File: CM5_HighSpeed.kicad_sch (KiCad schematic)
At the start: 60 parts, among them J1 USB-C, J10 USB-C, J15 USB_C_Receptacle, J17 USB-C, J22 Conn_HDMI, J5 Conn_1x22_Female, J6 USB-C, U11 TUSB4041I, U12 RT9742SNGV, U13 TLV73311PDBV, U15 AP22653W6, U6 AP22653W6, Y1 ECS-2520MV-240-CN-TR

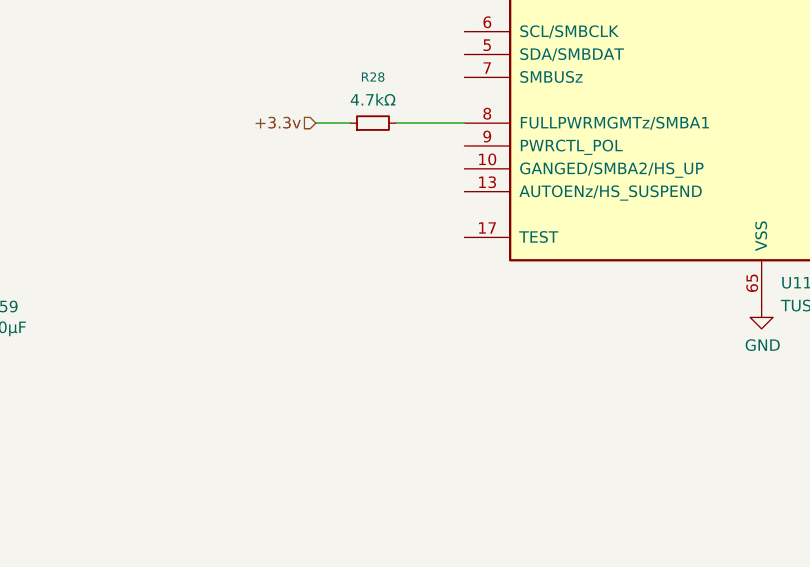
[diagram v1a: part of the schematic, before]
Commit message: USB hub: pull TEST (U11 pin 17) to GND through 4.7k
Pin 17 was left floating. It has an internal pull-down, but TI's
application circuit (TUSB4041I datasheet, Figure 7-8) pulls it down
externally with 4.7k, so follow the reference design.

New R47: 4.7k 1% 0603, Panasonic ERJ-3EKF4701V.

Refs #26 (verify on hardware before closing).

Co-Authored-By: Claude Opus 5.5 <noreply@anthropic.com>
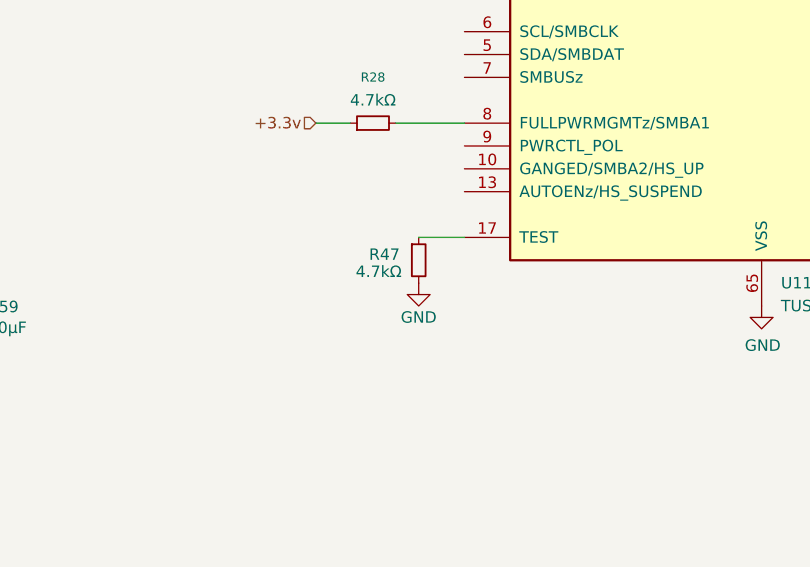
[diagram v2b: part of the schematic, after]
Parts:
- added R47: 4.7kΩ, Resistor_SMD:R_0603_1608Metric, symbol Device:R_Small
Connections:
- net GND: now also R47.2
- net at U11.17 (TEST): now also R47.1
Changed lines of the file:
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@@
 	(wire
 		(pts
+			(xy 210.82 204.47) (xy 215.9 204.47)
+		)
+		(stroke
+			(width 0)
+			(type default)
+		)
+	)
+	(wire
+		(pts
 			(xy 148.59 25.4) (xy 148.59 33.02)
 		)
@@
 	(symbol
 		(lib_id "power:GND")
+		(at 210.82 209.55 0)
+		(unit 1)
+		(body_style 1)
+		(exclude_from_sim no)
+		(in_bom yes)
+		(on_board yes)
+		(in_pos_files yes)
+		(dnp no)
+		(property "Reference" "#PWR002"
+			(at 210.82 215.9 0)
+			(hide yes)
+			(show_name no)
+			(do_not_autoplace no)
+			(effects
+				(font
+					(size 1.27 1.27)
+				)
+			)
+		)
+		(property "Value" "GND"
+			(at 210.82 213.36 0)
+			(show_name no)
+			(do_not_autoplace no)
+			(effects
+				(font
+					(size 1.27 1.27)
+				)
+			)
+		)
+		(property "Footprint" ""
+			(at 210.82 209.55 0)
+			(hide yes)
+			(show_name no)
+			(do_not_autoplace no)
+			(effects
+				(font
+					(size 1.27 1.27)
+				)
+			)
+		)
+		(property "Datasheet" ""
+			(at 210.82 209.55 0)
+			(hide yes)
+			(show_name no)
+			(do_not_autoplace no)
+			(effects
+				(font
+					(size 1.27 1.27)
+				)
+			)
+		)
+		(property "Description" "Power symbol creates a global label with name \"GND\" , ground"
+			(at 210.82 209.55 0)
+			(hide yes)
+			(show_name no)
+			(do_not_autoplace no)
+			(effects
+				(font
+					(size 1.27 1.27)
+				)
+			)
+		)
+		(pin "1"
+		)
+		(instances
+			(project "libreboard"
+				(path "/e63e39d7-6ac0-4ffd-8aa3-1841a4541b55/00000000-0000-0000-0000-00005cff70b1"
+					(reference "#PWR002")
+					(unit 1)
+				)
+			)
+		)
+	)
+	(symbol
+		(lib_id "power:GND")
 		(at 62.23 255.27 0)
 		(unit 1)
@@
 					(unit 1)
 				)
+			)
+		)
+	)
+	(symbol
+		(lib_id "Device:R_Small")
+		(at 210.82 207.01 0)
+		(unit 1)
+		(body_style 1)
+		(exclude_from_sim no)
+		(in_bom yes)
+		(on_board yes)
+		(in_pos_files yes)
+		(dnp no)
+		(property "Reference" "R47"
+			(at 207.01 206.375 0)
+			(show_name no)
+			(do_not_autoplace no)
+			(effects
+				(font
+					(size 1.27 1.27)
+				)
+			)
+		)
+		(property "Value" "4.7kΩ"
+			(at 206.375 208.28 0)
+			(show_name no)
+			(do_not_autoplace no)
+			(effects
+				(font
+					(size 1.27 1.27)
+				)
+			)
+		)
+		(property "Footprint" "Resistor_SMD:R_0603_1608Metric"
+			(at 210.82 207.01 0)
+			(hide yes)
+			(show_name no)
+			(do_not_autoplace no)
+			(effects
+				(font
+					(size 1.27 1.27)
+				)
+			)
+		)
+		(property "Datasheet" ""
+			(at 210.82 207.01 0)
+			(hide yes)
+			(show_name no)
+			(do_not_autoplace no)
+			(effects
+				(font
+					(size 1.27 1.27)
+				)
+			)
+		)
+		(property "Description" "Resistor, small symbol"
+			(at 210.82 207.01 0)
+			(hide yes)
+			(show_name no)
+			(do_not_autoplace no)
+			(effects
+				(font
+					(size 1.27 1.27)
+				)
+			)
+		)
+		(property "Dist. P/N" "P4.70KHTR-ND"
+			(at 210.82 207.01 0)
+			(hide yes)
+			(show_name no)
+			(do_not_autoplace no)
+			(effects
+				(font
+					(size 1.27 1.27)
+				)
+			)
+		)
+		(property "Distributor" "Digikey"
+			(at 210.82 207.01 0)
+			(hide yes)
+			(show_name no)
+			(do_not_autoplace no)
+			(effects
+				(font
+					(size 1.27 1.27)
+				)
+			)
+		)
+		(property "Manf. P/N" "ERJ-3EKF4701V"
+			(at 210.82 207.01 0)
+			(hide yes)
+			(show_name no)
+			(do_not_autoplace no)
+			(effects
+				(font
+					(size 1.27 1.27)
+				)
+			)
+		)
+		(property "Manufacturer" "Panasonic"
+			(at 210.82 207.01 0)
+			(hide yes)
+			(show_name no)
+			(do_not_autoplace no)
+			(effects
+				(font
+					(size 1.27 1.27)
+				)
+			)
+		)
+		(property "Part Description" "Resistor, 4.7kΩ, ±1%, 0.1W, SMD 0603 (1608m)"
+			(at 210.82 207.01 0)
+			(hide yes)
+			(show_name no)
+			(do_not_autoplace no)
+			(effects
+				(font
+					(size 1.27 1.27)
+				)
+			)
+		)
+		(pin "1"
+		)
+		(pin "2"
+		)
+		(instances
+			(project "libreboard"
+				(path "/e63e39d7-6ac0-4ffd-8aa3-1841a4541b55/00000000-0000-0000-0000-00005cff70b1"
+					(reference "R47")
+					(unit 1)
+				)

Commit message: USB hub: divide VBUS down before U11 USB_VBUS (pin 16)
U11 pin 16 was tied straight to the 5 V USB2_VBUS rail. Its absolute
maximum is 1.4 V and the recommended maximum 1.155 V (TUSB4041I
datasheet 5.1/5.3); the pin function table requires a 90.9k/10k 1%
divider. Continuous overstress of this pin is the most likely reason
the Rev1 hub worked for a while and then never enumerated again.

New R48 90.9k (ERJ-3EKF9092V) from USB2_VBUS and R49 10k (ERJ-3EKF1002V)
to GND, 0603; the midpoint feeds pin 16 through the HUB_VBUS_DET label.
5.0 V gives 0.495 V, 5.5 V gives 0.545 V at the pin.

Refs #23 (verify on hardware before closing).

Co-Authored-By: Claude Opus 5.5 <noreply@anthropic.com>
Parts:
- added R48: 90.9kΩ, Resistor_SMD:R_0603_1608Metric, symbol Device:R_Small
- added R49: 10kΩ, Resistor_SMD:R_0603_1608Metric, symbol Device:R_Small
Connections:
- net GND: now also R49.2
- net USB2_VBUS: now also R48.1; no longer U11.16 (USB_VBUS)
- new net HUB_VBUS_DET: R48.2, R49.1, U11.16 (USB_VBUS)

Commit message: USB hub: run the 24 MHz oscillator Y1 from the CM5 1.8 V output
Y1 (ECS-2520MV, 1.6-3.6 V supply) was powered from +3.3 V and drove
U11 XI (pin 30) with a 3.3 V clock. XI is rated 2.45 V absolute maximum
and TI requires a 1.8 V clock source (TUSB4041I datasheet 5.1, 6.3.6).

- Y1 VDD and its decoupling cap C50 move from +3.3v to a new +1V8 net.
- +1V8 comes from the CM5's +1.8 V output pins 88/90 (600 mA total),
  which were unused (no-connect flags removed).
- Y1 tri-state pin 1 gets a no-connect flag: open = output enabled per
  the ECS-2520MV datasheet.

Note: Y1's Value field says ECS-2520MV-240-CN-TR while its MPN/Digikey
fields say -DN-TR (C = +/-25 ppm, D = +/-20 ppm); both meet the hub's
+/-100 ppm. Left as is for the BOM owner to reconcile.

Refs #24 (verify on hardware before closing).

Co-Authored-By: Claude Opus 5.5 <noreply@anthropic.com>
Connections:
- net +3.3v: no longer C50.2, Y1.4 (VDD)
- new net +1V8: C50.2, Y1.4 (VDD)
- no-connect marks 3 -> 4
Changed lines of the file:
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@@
 		(at 254 66.04)
 	)
+	(no_connect
+		(at 151.13 160.02)
+	)
 	(wire
 		(pts
@@
 		)
 	)
-	(hierarchical_label "+3.3v"
-		(shape input)
-		(at 135.89 146.05 180)
-		(effects
-			(font
-				(size 1.27 1.27)
-			)
-			(justify right)
-		)
-	)
 	(hierarchical_label "PCIE_nCLKREQ"
 		(shape input)
@@
 					(unit 1)
 				)
+			)
+		)
+	)
+	(symbol
+		(lib_id "power:+1V8")
+		(at 135.89 146.05 0)
+		(unit 1)
+		(body_style 1)
+		(exclude_from_sim no)
+		(in_bom yes)
+		(on_board yes)
+		(in_pos_files yes)
+		(dnp no)
+		(property "Reference" "#PWR004"
+			(at 135.89 149.86 0)
+			(hide yes)
+			(show_name no)
+			(do_not_autoplace no)
+			(effects
+				(font
+					(size 1.27 1.27)
+				)
+			)
+		)
+		(property "Value" "+1V8"
+			(at 135.89 142.494 0)
+			(show_name no)
+			(do_not_autoplace no)
+			(effects
+				(font
+					(size 1.27 1.27)
+				)
+			)
+		)
+		(property "Footprint" ""
+			(at 135.89 146.05 0)
+			(hide yes)
+			(show_name no)
+			(do_not_autoplace no)
+			(effects
+				(font
+					(size 1.27 1.27)
+				)
+			)
+		)
+		(property "Datasheet" ""
+			(at 135.89 146.05 0)
+			(hide yes)
+			(show_name no)
+			(do_not_autoplace no)
+			(effects
+				(font
+					(size 1.27 1.27)
+				)
+			)
+		)
+		(property "Description" "Power symbol creates a global label with name \"+1V8\""
+			(at 135.89 146.05 0)
+			(hide yes)
+			(show_name no)
+			(do_not_autoplace no)
+			(effects
+				(font
+					(size 1.27 1.27)
+				)
+			)
+		)
+		(pin "1"
+		)
+		(instances
+			(project "libreboard"
+				(path "/e63e39d7-6ac0-4ffd-8aa3-1841a4541b55/00000000-0000-0000-0000-00005cff70b1"
+					(reference "#PWR004")
+					(unit 1)
+				)

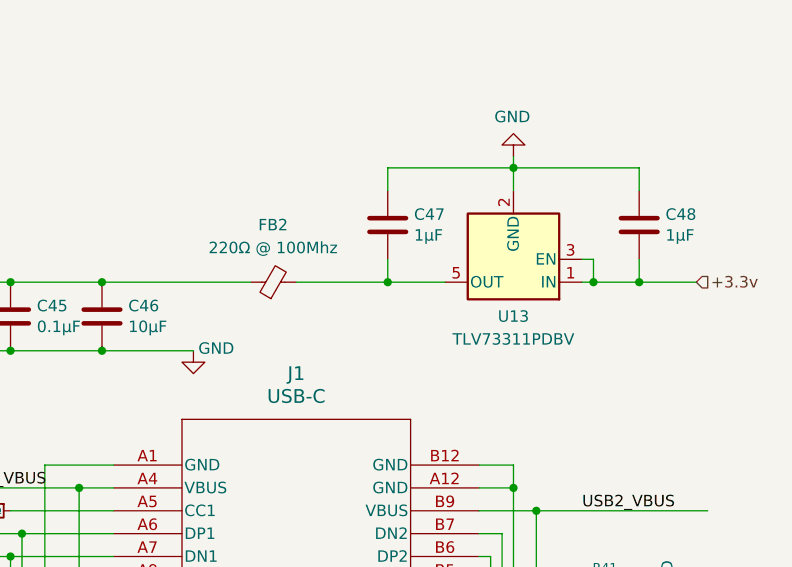
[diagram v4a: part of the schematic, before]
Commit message: USB hub: 1 A / 1.2 V core LDO enabled from 1.8 V, low-DCR core bead
- U13 TLV73311PDBV (300 mA, current limit 360 mA min) -> TLV75712PDBVR
  (1 A, 1.2 V, same SOT-23-5 pinout). The hub's VDD draws up to
  332-370 mA while held in reset (TUSB4041I rev F, 5.7), above what the
  old LDO could supply. TI allows a 1.2 V core supply (5.3 note 1:
  VDD 0.99-1.26 V). The symbol keeps its TLV73311PDBV library link
  (identical pins); use KiCad "Change Symbol" if the link should
  follow.
- U13 EN moves from +3.3v to +1V8 so the core rail, and therefore the
  hub's reset release, only starts after the oscillator Y1 is powered:
  3.3 V -> 1.8 V (Y1 runs) -> 1.2 V core -> reset release.
- FB2 LI0402C221R-10 (0.35 ohm DCR, 300 mA) -> Murata BLM18KG121TN1D
  (0603, 30 mohm DCR max, 3 A). TI asks for < 0.05 ohm on the core rail
  (7.3.1); the old bead dropped ~0.13 V at reset current.

Digikey numbers (296-50412-2-ND, 490-5254-2-ND) were not confirmed
against a live listing; check when ordering.

Refs #22 (verify on hardware before closing).

Co-Authored-By: Claude Opus 5.5 <noreply@anthropic.com>
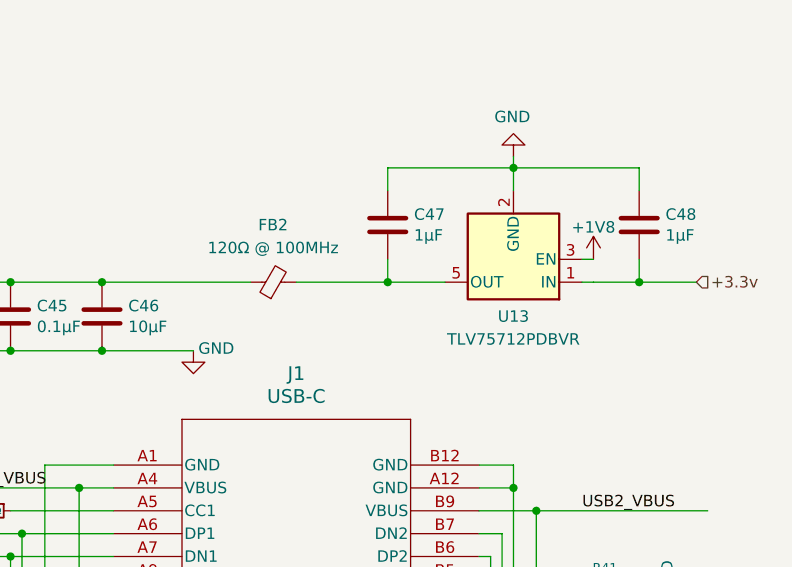
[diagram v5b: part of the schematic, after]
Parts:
- FB2: value 220Ω @ 100Mhz -> 120Ω @ 100MHz; footprint libreboard:BEADC1005X55N -> Inductor_SMD:L_0603_1608Metric; Dist. P/N 240-2554-2-ND -> 490-5254-2-ND; Manf. P/N LI0402C221R-10 -> BLM18KG121TN1D; Manufacturer Laird Signal -> Murata; Part Description Filter, Ferrite Bead, 220Ω @ 100MHz, SMD 0402 -> Filter, Ferrite Bead, 120Ω @ 100MHz, 3A, 30mΩ DCR max, SMD 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
- U13: value TLV73311PDBV -> TLV75712PDBVR; Dist. P/N 296-38620-2-ND -> 296-50412-2-ND; Manf. P/N TLV73311PDBVT -> TLV75712PDBVR; Part Description LVR, IC Positive Fixed, 1 Output, 300mA, SOT-23-5 -> LDO, fixed 1.2 V, 1 A, SOT-23-5
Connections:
- net +1V8: now also U13.3 (EN)
- net +3.3v: no longer U13.3 (EN)
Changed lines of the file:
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@@
 	)
 	(junction
-		(at 389.89 99.06)
-		(diameter 0)
-		(color 0 0 0 0)
-	)
-	(junction
 		(at 381 156.21)
 		(diameter 0)
@@
 	(wire
 		(pts
-			(xy 389.89 96.52) (xy 389.89 99.06)
-		)
-		(stroke
-			(width 0)
-			(type default)
-		)
-	)
-	(wire
-		(pts
 			(xy 99.06 93.98) (xy 101.6 93.98)
 		)
@@
 			)
 		)
-		(property "Value" "220Ω @ 100Mhz"
+		(property "Value" "120Ω @ 100MHz"
 			(at 354.2919 95.25 90)
 			(show_name no)
@@
 			)
 		)
-		(property "Footprint" "libreboard:BEADC1005X55N"
+		(property "Footprint" "Inductor_SMD:L_0603_1608Metric"
 			(at 354.33 100.838 90)
 			(hide yes)
@@
 			)
 		)
-		(property "Datasheet" ""
+		(property "Datasheet" "https://www.murata.com/en-us/products/productdetail?partno=BLM18KG121TN1%23"
 			(at 354.33 99.06 0)
 			(hide yes)
@@
 			)
 		)
-		(property "Dist. P/N" "240-2554-2-ND"
+		(property "Dist. P/N" "490-5254-2-ND"
 			(at 354.33 99.06 90)
 			(hide yes)
@@
 			)
 		)
-		(property "Manf. P/N" "LI0402C221R-10"
+		(property "Manf. P/N" "BLM18KG121TN1D"
 			(at 354.33 99.06 90)
 			(hide yes)
@@
 			)
 		)
-		(property "Manufacturer" "Laird Signal"
+		(property "Manufacturer" "Murata"
 			(at 354.33 99.06 90)
 			(hide yes)
@@
 			)
 		)
-		(property "Part Description" "Filter, Ferrite Bead, 220Ω @ 100MHz, SMD 0402"
+		(property "Part Description" "Filter, Ferrite Bead, 120Ω @ 100MHz, 3A, 30mΩ DCR max, SMD 0603 (1608m)"
 			(at 354.33 99.06 90)
 			(hide yes)
@@
 			)
 		)
-		(property "Value" "TLV73311PDBV"
+		(property "Value" "TLV75712PDBVR"
 			(at 381 105.41 0)
 			(show_name no)
@@
 			)
 		)
-		(property "Datasheet" "http://www.ti.com/lit/ds/symlink/tlv733p.pdf"
+		(property "Datasheet" "https://www.ti.com/lit/ds/symlink/tlv757p.pdf"
 			(at 381 96.52 0)
 			(hide yes)
@@
 			)
 		)
-		(property "Description" "300mA Capacitor-Free Low Dropout Voltage Regulator, Fixed Output 1.1V, SOT-23-5"
+		(property "Description" "1 A low-dropout regulator, fixed 1.2 V output, SOT-23-5"
 			(at 381 96.52 0)
 			(hide yes)
@@
 			)
 		)
-		(property "Dist. P/N" "296-38620-2-ND"
+		(property "Dist. P/N" "296-50412-2-ND"
 			(at 381 96.52 0)
 			(hide yes)
@@
 			)
 		)
-		(property "Manf. P/N" "TLV73311PDBVT"
+		(property "Manf. P/N" "TLV75712PDBVR"
 			(at 381 96.52 0)
 			(hide yes)
@@
 			)
 		)
-		(property "Part Description" "LVR, IC Positive Fixed, 1 Output, 300mA, SOT-23-5"
+		(property "Part Description" "LDO, fixed 1.2 V, 1 A, SOT-23-5"
 			(at 381 96.52 0)
 			(hide yes)
@@
 					(unit 1)
 				)
+			)
+		)
+	)
+	(symbol
+		(lib_id "power:+1V8")
+		(at 389.89 96.52 0)
+		(unit 1)
+		(body_style 1)
+		(exclude_from_sim no)
+		(in_bom yes)
+		(on_board yes)
+		(in_pos_files yes)
+		(dnp no)
+		(property "Reference" "#PWR005"
+			(at 389.89 100.33 0)
+			(hide yes)
+			(show_name no)
+			(do_not_autoplace no)
+			(effects
+				(font
+					(size 1.27 1.27)
+				)
+			)
+		)
+		(property "Value" "+1V8"
+			(at 389.89 92.964 0)
+			(show_name no)
+			(do_not_autoplace no)
+			(effects
+				(font
+					(size 1.27 1.27)
+				)
+			)
+		)
+		(property "Footprint" ""
+			(at 389.89 96.52 0)
+			(hide yes)
+			(show_name no)
+			(do_not_autoplace no)
+			(effects
+				(font
+					(size 1.27 1.27)
+				)
+			)
+		)
+		(property "Datasheet" ""
+			(at 389.89 96.52 0)
+			(hide yes)
+			(show_name no)
+			(do_not_autoplace no)
+			(effects
+				(font
+					(size 1.27 1.27)
+				)
+			)
+		)
+		(property "Description" "Power symbol creates a global label with name \"+1V8\""
+			(at 389.89 96.52 0)
+			(hide yes)
+			(show_name no)
+			(do_not_autoplace no)
+			(effects
+				(font
+					(size 1.27 1.27)
+				)
+			)
+		)
+		(pin "1"
+		)
+		(instances
+			(project "libreboard"
+				(path "/e63e39d7-6ac0-4ffd-8aa3-1841a4541b55/00000000-0000-0000-0000-00005cff70b1"
+					(reference "#PWR005")
+					(unit 1)
+				)
